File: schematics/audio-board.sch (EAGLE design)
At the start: 50 parts, among them K1 351, K2 351, Q1 BSS138, Q2 BSS138, T1 BC547, T2 BC547, U1 TDA1543, U2 PT2322-S

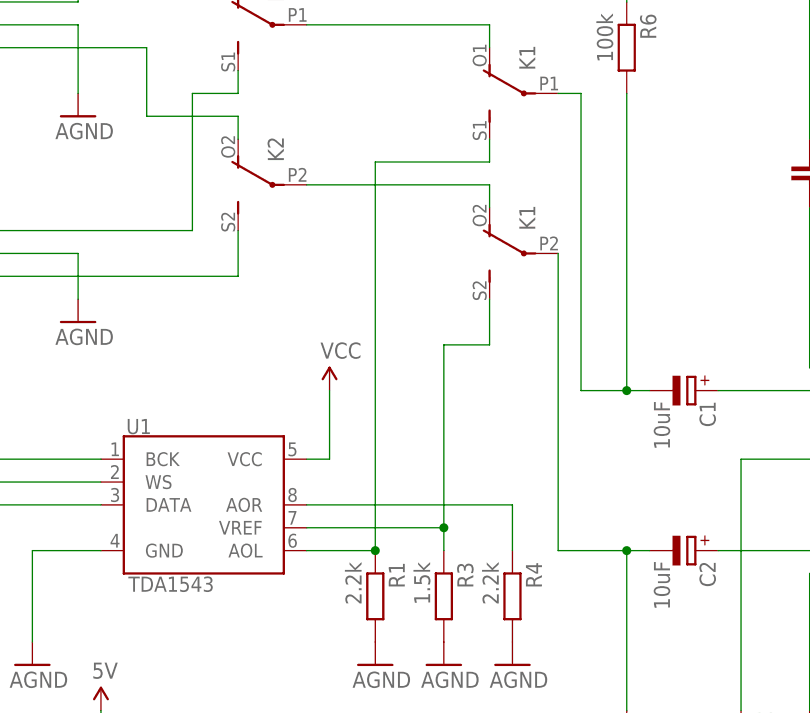
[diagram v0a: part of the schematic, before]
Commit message: corrected error in audio board schematics
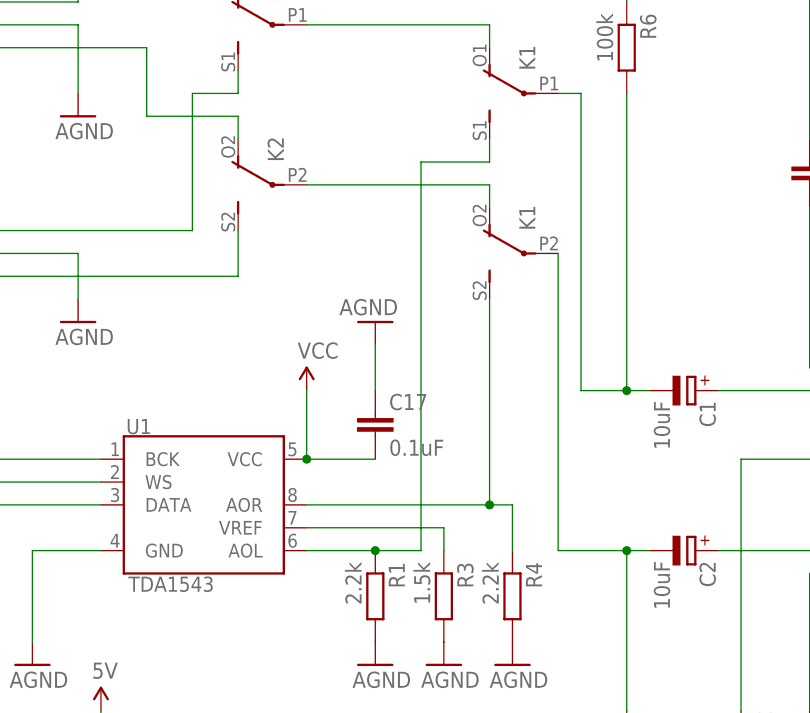
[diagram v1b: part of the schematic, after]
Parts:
- added C17: 0.1uF, rcl:C-EU025-025X050
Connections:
- net AGND: now also C17.1
- net N$33: now also K13.S
- net N$36: no longer K13.S
- net VCC: now also C17.2
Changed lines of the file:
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@@
 <?xml version="1.0" encoding="utf-8"?>
 <!DOCTYPE eagle SYSTEM "eagle.dtd">
-<eagle version="7.5.0">
+<eagle version="7.6.0">
 <drawing>
 <settings>
@@
 <part name="U$19" library="SparkFun-Aesthetics" deviceset="AGND" device=""/>
 <part name="U$2" library="SparkFun-Aesthetics" deviceset="AGND" device=""/>
+<part name="C17" library="rcl" deviceset="C-EU" device="025-025X050" value="0.1uF"/>
+<part name="U$20" library="SparkFun-Aesthetics" deviceset="AGND" device=""/>
 </parts>
 <sheets>
@@
 <instance part="R3" gate="G$1" x="58.42" y="33.02" rot="R270"/>
 <instance part="R4" gate="G$1" x="66.04" y="33.02" rot="R270"/>
-<instance part="SUPPLY2" gate="1" x="45.72" y="55.88"/>
+<instance part="SUPPLY2" gate="1" x="43.18" y="55.88"/>
 <instance part="T2" gate="G$1" x="66.04" y="-7.62" rot="MR0"/>
 <instance part="T1" gate="G$1" x="45.72" y="-25.4" rot="MR0"/>
@@
 <instance part="U$19" gate="G$1" x="109.22" y="43.18"/>
 <instance part="U$2" gate="G$1" x="218.44" y="38.1"/>
+<instance part="C17" gate="G$1" x="50.8" y="53.34"/>
+<instance part="U$20" gate="G$1" x="50.8" y="63.5" rot="R180"/>
 </instances>
 <busses>
@@
 <segment>
 <pinref part="U1" gate="G$1" pin="VCC"/>
-<wire x1="43.18" y1="48.26" x2="45.72" y2="48.26" width="0.2032" layer="91"/>
-<wire x1="45.72" y1="48.26" x2="45.72" y2="55.88" width="0.2032" layer="91"/>
+<wire x1="43.18" y1="48.26" x2="43.18" y2="55.88" width="0.2032" layer="91"/>
 <pinref part="SUPPLY2" gate="1" pin="VCC"/>
+<pinref part="C17" gate="G$1" pin="2"/>
+<wire x1="43.18" y1="48.26" x2="50.8" y2="48.26" width="0.2032" layer="91"/>
+<junction x="43.18" y="48.26"/>
 </segment>
 <segment>
@@
 <segment>
 <pinref part="U1" gate="G$1" pin="AOR"/>
-<wire x1="43.18" y1="43.18" x2="66.04" y2="43.18" width="0.2032" layer="91"/>
+<wire x1="43.18" y1="43.18" x2="63.5" y2="43.18" width="0.2032" layer="91"/>
 <pinref part="R4" gate="G$1" pin="1"/>
+<wire x1="63.5" y1="43.18" x2="66.04" y2="43.18" width="0.2032" layer="91"/>
 <wire x1="66.04" y1="43.18" x2="66.04" y2="38.1" width="0.2032" layer="91"/>
+<pinref part="K1" gate="3" pin="S"/>
+<wire x1="63.5" y1="66.04" x2="63.5" y2="43.18" width="0.2032" layer="91"/>
+<junction x="63.5" y="43.18"/>
 </segment>
 </net>
@@
 <pinref part="U1" gate="G$1" pin="AOL"/>
 <wire x1="43.18" y1="38.1" x2="50.8" y2="38.1" width="0.2032" layer="91"/>
-<wire x1="50.8" y1="38.1" x2="50.8" y2="81.28" width="0.2032" layer="91"/>
+<wire x1="50.8" y1="38.1" x2="55.88" y2="38.1" width="0.2032" layer="91"/>
+<wire x1="55.88" y1="38.1" x2="55.88" y2="81.28" width="0.2032" layer="91"/>
 <junction x="50.8" y="38.1"/>
-<wire x1="50.8" y1="81.28" x2="63.5" y2="81.28" width="0.2032" layer="91"/>
+<wire x1="55.88" y1="81.28" x2="63.5" y2="81.28" width="0.2032" layer="91"/>
 <pinref part="K1" gate="2" pin="S"/>
 <wire x1="63.5" y1="81.28" x2="63.5" y2="83.82" width="0.2032" layer="91"/>
@@
 <net name="N$36" class="0">
 <segment>
-<pinref part="K1" gate="3" pin="S"/>
-<wire x1="63.5" y1="66.04" x2="63.5" y2="60.96" width="0.2032" layer="91"/>
-<wire x1="63.5" y1="60.96" x2="58.42" y2="60.96" width="0.2032" layer="91"/>
 <pinref part="U1" gate="G$1" pin="VREF"/>
 <wire x1="43.18" y1="40.64" x2="58.42" y2="40.64" width="0.2032" layer="91"/>
 <pinref part="R3" gate="G$1" pin="1"/>
 <wire x1="58.42" y1="40.64" x2="58.42" y2="38.1" width="0.2032" layer="91"/>
-<wire x1="58.42" y1="60.96" x2="58.42" y2="40.64" width="0.2032" layer="91"/>
-<junction x="58.42" y="40.64"/>
 </segment>
 </net>
@@
 <wire x1="12.7" y1="38.1" x2="12.7" y2="27.94" width="0.2032" layer="91"/>
 </segment>
-</net>
+<segment>
+<pinref part="C17" gate="G$1" pin="1"/>
+<pinref part="U$20" gate="G$1" pin="AGND"/>
+<wire x1="50.8" y1="60.96" x2="50.8" y2="55.88" width="0.2032" layer="91"/>
+</segment>
+</net>
